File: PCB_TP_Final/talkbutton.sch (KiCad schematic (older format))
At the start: 6 parts, among them SW1 SW_Push

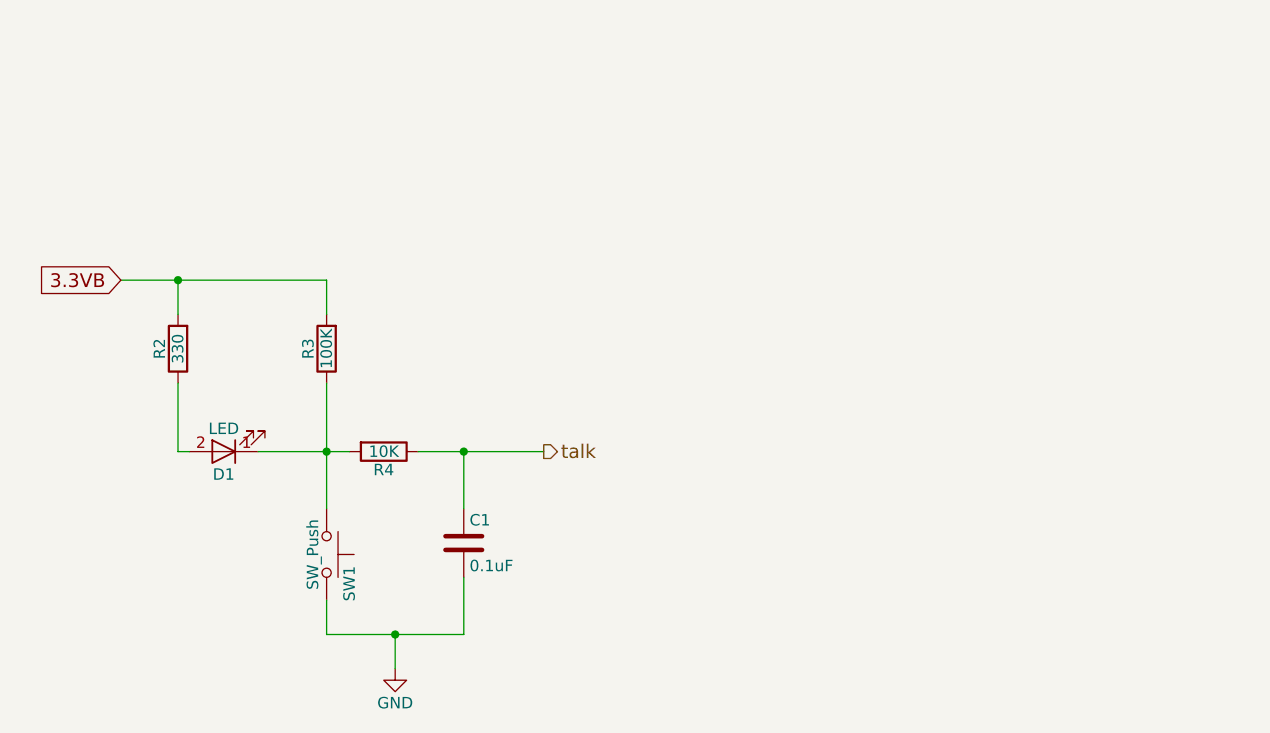
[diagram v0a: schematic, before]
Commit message: Se agregaron correcciones sugeridas
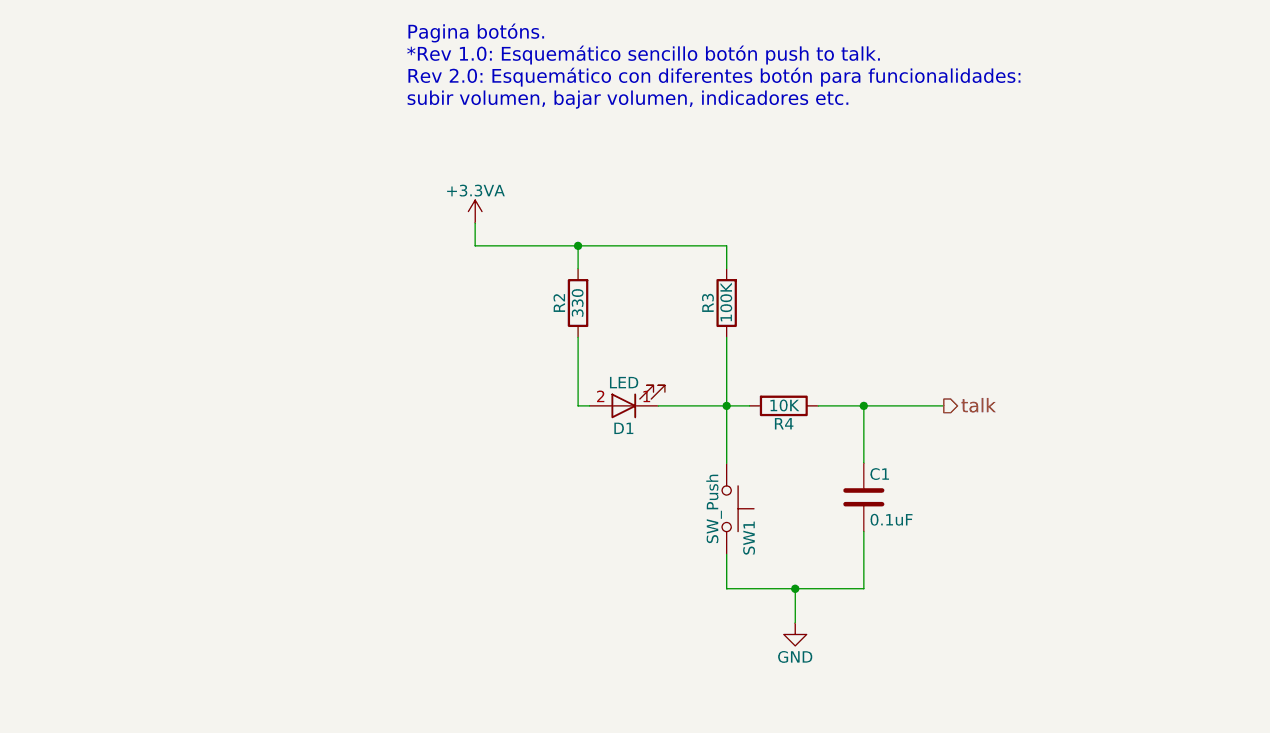
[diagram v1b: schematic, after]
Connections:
- net 3.3VB renamed +3.3VA
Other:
- note added: "Pagina botóns.\n*Rev 1.0: Esquemático sencillo botón push to talk.\nRev 2.0: Esquemático con diferentes botón para funcionalidades:\nsubir volumen, bajar volumen, indicadores etc."
- moved on the sheet: C1, D1, R2, R3, R4, SW1
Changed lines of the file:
@@
 encoding utf-8
 Sheet 5 5
-Title ""
-Date ""
-Rev ""
-Comp ""
+Title "Circuit Push to Talk"
+Date "2018-10-19"
+Rev "1.0"
+Comp "Ericson Joseph Estupiñan Pineda"
 Comment1 ""
 Comment2 ""
@@
 Comment4 ""
 $EndDescr
-Text HLabel 5350 4000 2    60   Output ~ 0
+Text HLabel 7100 3800 2    60   Output ~ 0
 talk
 $Comp
-L GND #PWR08
+L GND #PWR011
 U 1 1 5BBD7417
-P 4700 4950
-F 0 "#PWR08" H 4700 4700 50  0001 C CNN
-F 1 "GND" H 4700 4800 50  0000 C CNN
-F 2 "" H 4700 4950 50  0001 C CNN
-F 3 "" H 4700 4950 50  0001 C CNN
-	1    4700 4950
+P 6450 4750
+F 0 "#PWR011" H 6450 4500 50  0001 C CNN
+F 1 "GND" H 6450 4600 50  0000 C CNN
+F 2 "" H 6450 4750 50  0001 C CNN
+F 3 "" H 6450 4750 50  0001 C CNN
+	1    6450 4750
 	1    0    0    -1
 $EndComp
@@
 L C C1
 U 1 1 5BBD742B
-P 5000 4400
-F 0 "C1" H 5025 4500 50  0000 L CNN
-F 1 "0.1uF" H 5025 4300 50  0000 L CNN
-F 2 "Capacitors_SMD:C_0805_HandSoldering" H 5038 4250 50  0001 C CNN
-F 3 "" H 5000 4400 50  0001 C CNN
-	1    5000 4400
+P 6750 4200
+F 0 "C1" H 6775 4300 50  0000 L CNN
+F 1 "0.1uF" H 6775 4100 50  0000 L CNN
+F 2 "Capacitors_SMD:C_0805_HandSoldering" H 6788 4050 50  0001 C CNN
+F 3 "" H 6750 4200 50  0001 C CNN
+	1    6750 4200
 	1    0    0    -1
 $EndComp
-Text GLabel 3500 3250 0    60   Input ~ 0
-3.3VB
 $Comp
 L R R4
 U 1 1 5BBD7B14
-P 4650 4000
-F 0 "R4" V 4730 4000 50  0000 C CNN
-F 1 "10K" V 4650 4000 50  0000 C CNN
-F 2 "Resistors_SMD:R_1206_HandSoldering" V 4580 4000 50  0001 C CNN
-F 3 "" H 4650 4000 50  0001 C CNN
-	1    4650 4000
+P 6400 3800
+F 0 "R4" V 6480 3800 50  0000 C CNN
+F 1 "10K" V 6400 3800 50  0000 C CNN
+F 2 "Resistors_SMD:R_1206_HandSoldering" V 6330 3800 50  0001 C CNN
+F 3 "" H 6400 3800 50  0001 C CNN
+	1    6400 3800
 	0    1    1    0
 $EndComp
@@
 L R R3
 U 1 1 5BBD7BA5
-P 4400 3550
-F 0 "R3" V 4480 3550 50  0000 C CNN
-F 1 "100K" V 4400 3550 50  0000 C CNN
-F 2 "Resistors_SMD:R_1206_HandSoldering" V 4330 3550 50  0001 C CNN
-F 3 "" H 4400 3550 50  0001 C CNN
-	1    4400 3550
+P 6150 3350
+F 0 "R3" V 6230 3350 50  0000 C CNN
+F 1 "100K" V 6150 3350 50  0000 C CNN
+F 2 "Resistors_SMD:R_1206_HandSoldering" V 6080 3350 50  0001 C CNN
+F 3 "" H 6150 3350 50  0001 C CNN
+	1    6150 3350
 	-1   0    0    1
 $EndComp
@@
 L R R2
 U 1 1 5BBD7E14
-P 3750 3550
-F 0 "R2" V 3830 3550 50  0000 C CNN
-F 1 "330" V 3750 3550 50  0000 C CNN
-F 2 "Resistors_SMD:R_1206_HandSoldering" V 3680 3550 50  0001 C CNN
-F 3 "" H 3750 3550 50  0001 C CNN
-	1    3750 3550
+P 5500 3350
+F 0 "R2" V 5580 3350 50  0000 C CNN
+F 1 "330" V 5500 3350 50  0000 C CNN
+F 2 "Resistors_SMD:R_1206_HandSoldering" V 5430 3350 50  0001 C CNN
+F 3 "" H 5500 3350 50  0001 C CNN
+	1    5500 3350
 	-1   0    0    1
 $EndComp
@@
 L LED D1
 U 1 1 5BBD7EBE
-P 3950 4000
-F 0 "D1" H 3950 4100 50  0000 C CNN
-F 1 "LED" H 3950 3900 50  0000 C CNN
-F 2 "LEDs:LED_0805_HandSoldering" H 3950 4000 50  0001 C CNN
-F 3 "" H 3950 4000 50  0001 C CNN
-	1    3950 4000
+P 5700 3800
+F 0 "D1" H 5700 3900 50  0000 C CNN
+F 1 "LED" H 5700 3700 50  0000 C CNN
+F 2 "LEDs:LED_0805_HandSoldering" H 5700 3800 50  0001 C CNN
+F 3 "" H 5700 3800 50  0001 C CNN
+	1    5700 3800
 	-1   0    0    1
 $EndComp
 Wire Wire Line
-	3750 4000 3800 4000
+	5500 3800 5550 3800
 Wire Wire Line
-	3750 3700 3750 4000
-Connection ~ 3750 3250
+	5500 3500 5500 3800
+Connection ~ 6750 3800
 Wire Wire Line
-	3750 3400 3750 3250
+	6750 4050 6750 3800
 Wire Wire Line
-	4400 3250 4400 3400
-Wire Wire Line
-	3500 3250 4400 3250
-Connection ~ 5000 4000
-Wire Wire Line
-	5000 4250 5000 4000
-Wire Wire Line
-	4800 4000 5350 4000
+	6550 3800 7100 3800
 $Comp
 L SW_Push SW1
 U 1 1 5BBDB115
-P 4400 4450
-F 0 "SW1" H 4450 4550 50  0000 L CNN
-F 1 "SW_Push" H 4400 4390 50  0000 C CNN
-F 2 "Buttons_Switches_THT:SW_PUSH_6mm_h8mm" H 4400 4650 50  0001 C CNN
-F 3 "" H 4400 4650 50  0001 C CNN
-	1    4400 4450
+P 6150 4250
+F 0 "SW1" H 6200 4350 50  0000 L CNN
+F 1 "SW_Push" H 6150 4190 50  0000 C CNN
+F 2 "Buttons_Switches_THT:SW_PUSH_6mm_h8mm" H 6150 4450 50  0001 C CNN
+F 3 "" H 6150 4450 50  0001 C CNN
+	1    6150 4250
 	0    1    1    0
 $EndComp
 Wire Wire Line
-	4400 4650 4400 4800
+	6150 4450 6150 4600
 Wire Wire Line
-	4400 4800 5000 4800
+	6150 4600 6750 4600
 Wire Wire Line
-	5000 4800 5000 4550
+	6750 4600 6750 4350
 Wire Wire Line
-	4700 4950 4700 4800
-Connection ~ 4700 4800
+	6450 4750 6450 4600
+Connection ~ 6450 4600
 Wire Wire Line
-	4400 4250 4400 3700
+	6150 4050 6150 3500
 Wire Wire Line
-	4100 4000 4500 4000
-Connection ~ 4400 4000
+	5850 3800 6250 3800
+Connection ~ 6150 3800
+$Comp
+L +3.3VA #PWR012
+U 1 1 5BCA8311
+P 5050 3000
+F 0 "#PWR012" H 5050 2850 50  0001 C CNN
+F 1 "+3.3VA" H 5050 3140 50  0000 C CNN
+F 2 "" H 5050 3000 50  0001 C CNN
+F 3 "" H 5050 3000 50  0001 C CNN
+	1    5050 3000
+	1    0    0    -1
+$EndComp
+Wire Wire Line
+	5050 3000 5050 3100
+Wire Wire Line
+	5050 3100 6150 3100
+Wire Wire Line
+	6150 3100 6150 3200
+Wire Wire Line
+	5500 3200 5500 3100
+Connection ~ 5500 3100
+Text Notes 4750 2500 0    60   ~ 0
+Pagina botóns.\n*Rev 1.0: Esquemático sencillo botón push to talk.\nRev 2.0: Esquemático con diferentes botón para funcionalidades:\nsubir volumen, bajar volumen, indicadores etc.
 $EndSCHEMATC
